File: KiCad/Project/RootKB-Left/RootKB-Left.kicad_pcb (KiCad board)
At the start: 2 copper layers, 137.4 x 107.4 mm, 70 parts, among them J1 OLED-128x32, SW1 Switch, U1 Arduino_Pro_Micro, U2 TRRS

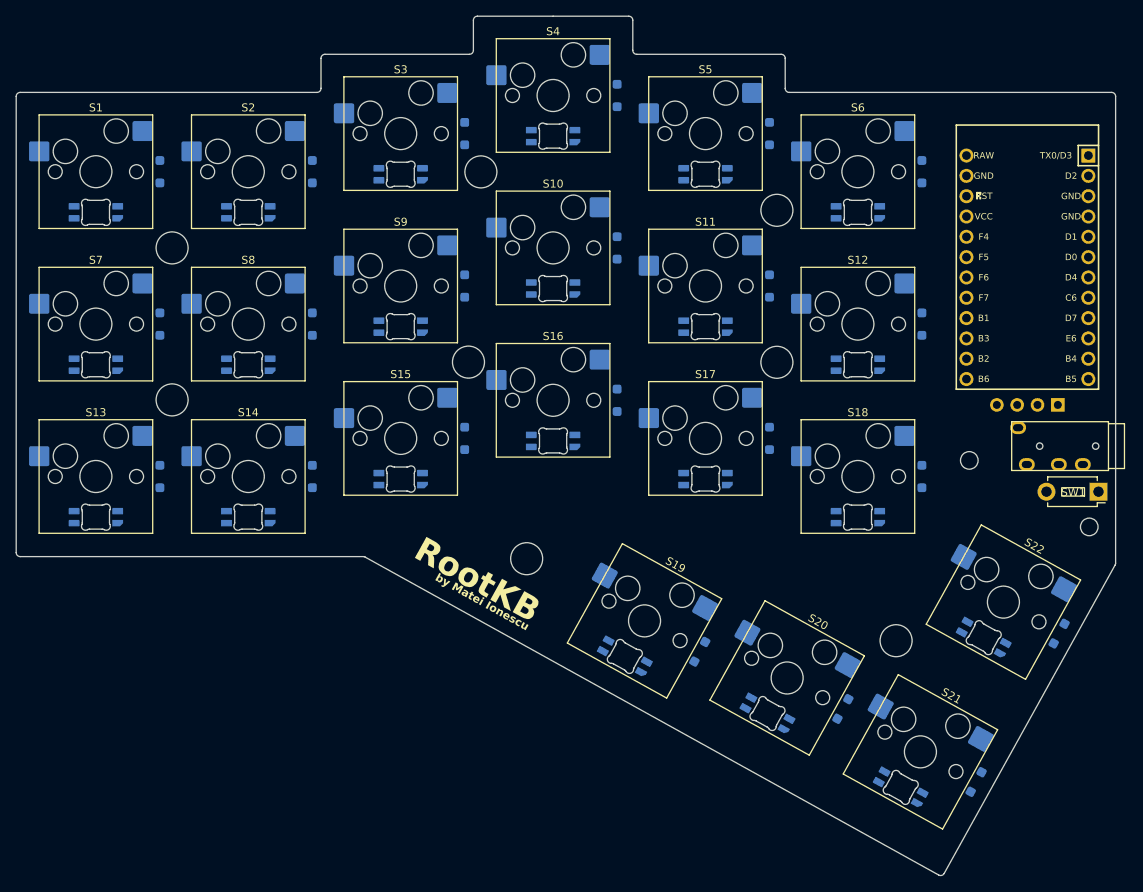
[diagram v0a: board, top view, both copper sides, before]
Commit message: route left
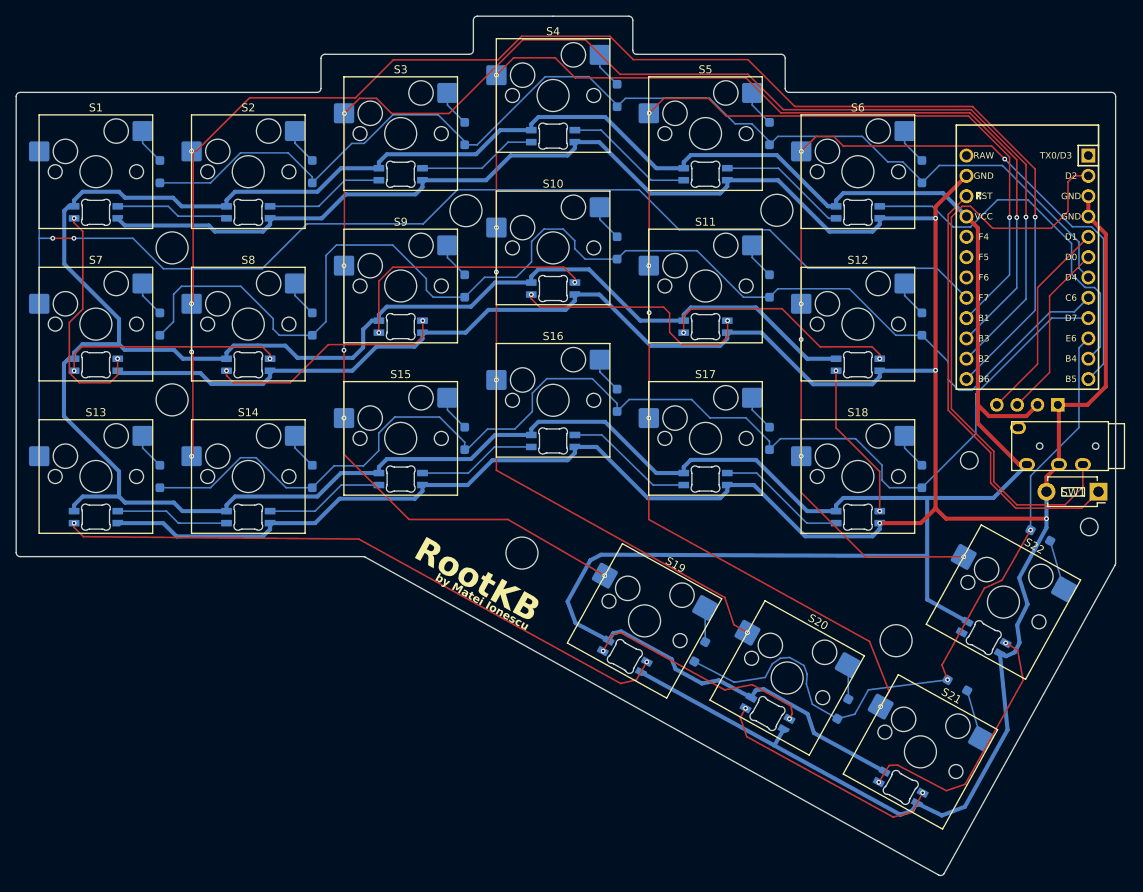
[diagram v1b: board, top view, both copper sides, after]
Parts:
- moved D22 12.5 mm to (203.8, 107.4), turned to -29 degrees
- moved D21 12.3 mm to (193.4, 126.1), turned to -29 degrees
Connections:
- LED1 pad 3: LED -> Net-(LED1-DIN)
- LED11 pad 2: Net-(LED10-DIN) -> Net-(LED11-DOUT)
- LED11 pad 3: Net-(LED11-DIN) -> Net-(LED10-DOUT)
- LED12 pad 2: Net-(LED11-DIN) -> Net-(LED12-DOUT)
- LED12 pad 3: Net-(LED12-DIN) -> Net-(LED11-DOUT)
- LED13 pad 4: unconnected-(LED13-VSS-Pad4) -> GND
- LED14 pad 2: Net-(LED14-DOUT) -> Net-(LED13-DIN)
- LED14 pad 3: Net-(LED13-DOUT) -> Net-(LED14-DIN)
- LED14 pad 4: unconnected-(LED14-VSS-Pad4) -> GND
- LED15 pad 2: Net-(LED15-DOUT) -> Net-(LED14-DIN)
- LED15 pad 3: Net-(LED14-DOUT) -> Net-(LED15-DIN)
- LED16 pad 2: Net-(LED16-DOUT) -> Net-(LED15-DIN)
- LED16 pad 3: Net-(LED15-DOUT) -> Net-(LED16-DIN)
- LED17 pad 2: Net-(LED17-DOUT) -> Net-(LED16-DIN)
- LED17 pad 3: Net-(LED16-DOUT) -> Net-(LED17-DIN)
- LED18 pad 2: Net-(LED18-DOUT) -> Net-(LED17-DIN)
- LED18 pad 3: Net-(LED17-DOUT) -> Net-(LED12-DOUT)
- LED19 pad 2: unconnected-(LED19-DOUT-Pad2) -> Net-(LED19-DOUT)
- LED19 pad 3: Net-(LED19-DIN) -> Net-(LED13-DOUT)
- LED2 pad 2: Net-(LED2-DOUT) -> Net-(LED1-DIN)
- LED2 pad 3: Net-(LED1-DOUT) -> Net-(LED2-DIN)
- LED20 pad 2: Net-(LED19-DIN) -> Net-(LED20-DOUT)
- LED20 pad 3: Net-(LED20-DIN) -> Net-(LED19-DOUT)
- LED21 pad 2: Net-(LED20-DIN) -> Net-(LED21-DOUT)
- LED21 pad 3: Net-(LED21-DIN) -> Net-(LED20-DOUT)
- LED22 pad 2: Net-(LED21-DIN) -> unconnected-(LED22-DOUT-Pad2)
- LED22 pad 3: Net-(LED18-DOUT) -> Net-(LED21-DOUT)
- LED3 pad 2: Net-(LED3-DOUT) -> Net-(LED2-DIN)
- LED3 pad 3: Net-(LED2-DOUT) -> Net-(LED3-DIN)
- LED4 pad 2: Net-(LED4-DOUT) -> Net-(LED3-DIN)
- LED4 pad 3: Net-(LED3-DOUT) -> Net-(LED4-DIN)
- LED5 pad 2: Net-(LED5-DOUT) -> Net-(LED4-DIN)
- LED5 pad 3: Net-(LED4-DOUT) -> Net-(LED5-DIN)
- LED6 pad 2: Net-(LED12-DIN) -> Net-(LED5-DIN)
- LED6 pad 3: Net-(LED5-DOUT) -> LED
- LED7 pad 2: Net-(LED13-DIN) -> Net-(LED7-DOUT)
- LED7 pad 3: Net-(LED7-DIN) -> Net-(LED1-DOUT)
- LED8 pad 2: Net-(LED7-DIN) -> Net-(LED8-DOUT)
- LED8 pad 3: Net-(LED8-DIN) -> Net-(LED7-DOUT)
- LED9 pad 2: Net-(LED8-DIN) -> Net-(LED10-DIN)
- LED9 pad 3: Net-(LED10-DOUT) -> Net-(LED8-DOUT)
- U1 pad 13: Column 4 -> Column 1
- U1 pad 14: Column 3 -> Column 2
- U1 pad 15: Column 2 -> Column 3
- U1 pad 16: Column 1 -> Column 4
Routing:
- net VCC: track 0.00 -> 579.8 mm
- net GND: track 0.00 -> 544.0 mm, vias 0 -> 4
- net Column 2: track 0.00 -> 205.0 mm, vias 0 -> 6
- net Column 1: track 0.00 -> 186.6 mm, vias 0 -> 5
- net Column 3: track 0.00 -> 184.2 mm, vias 0 -> 6
- net Column 0: track 0.00 -> 165.3 mm, vias 0 -> 2
- net Column 4: track 0.00 -> 162.5 mm, vias 0 -> 6
- net Row 1: track 0.00 -> 158.8 mm
- net Row 2: track 0.00 -> 153.4 mm
- net Row 0: track 0.00 -> 144.8 mm
- net Column 5: track 0.00 -> 128.5 mm, vias 0 -> 6
- net Row 3: track 0.00 -> 89.8 mm, vias 0 -> 2
- net Net-(LED13-DOUT): track 0.00 -> 78.6 mm, vias 0 -> 2
- net TRRS_SERIAL: track 0.00 -> 75.0 mm
- net RST: track 0.00 -> 54.9 mm
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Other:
- outline, holes or cut-outs redrawn

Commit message: routing left
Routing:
- net Column 2: track 205.0 -> 203.4 mm

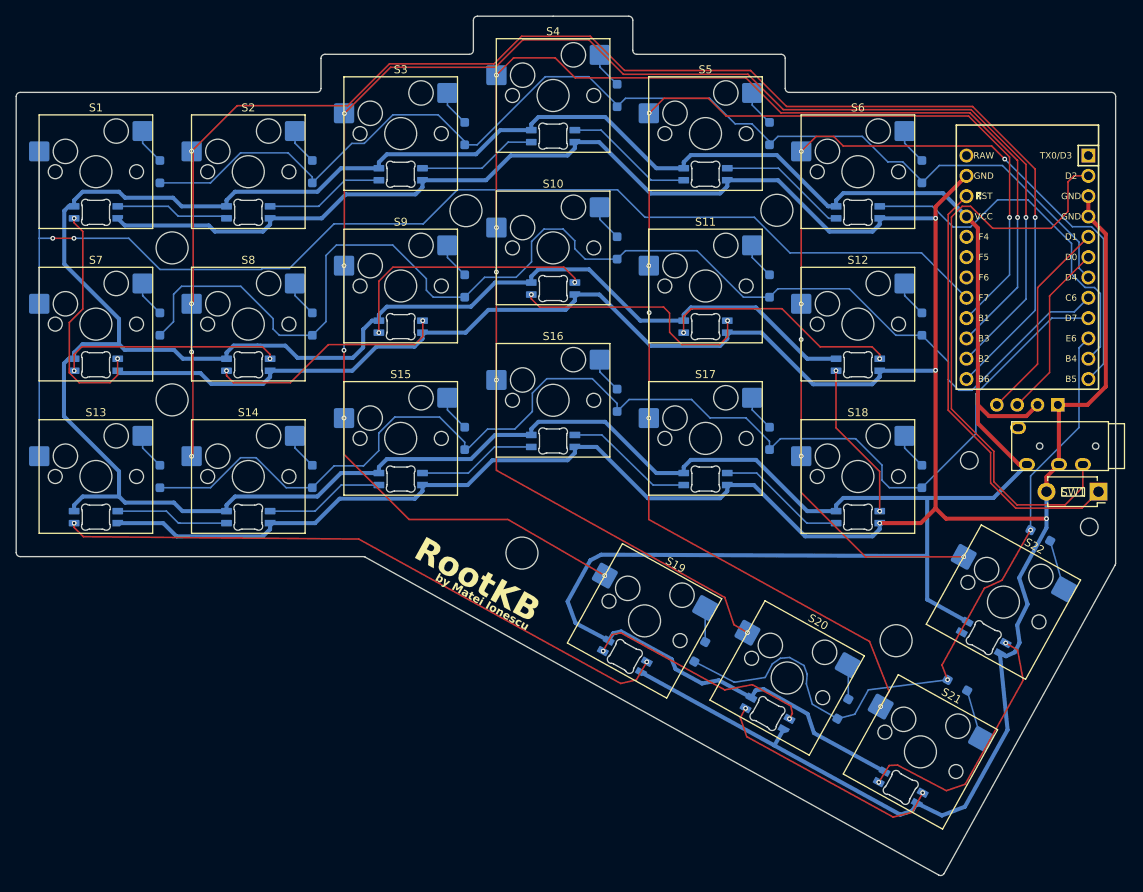
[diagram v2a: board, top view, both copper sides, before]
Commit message: remove reset button
also use real Arduino ProMicro dimensions
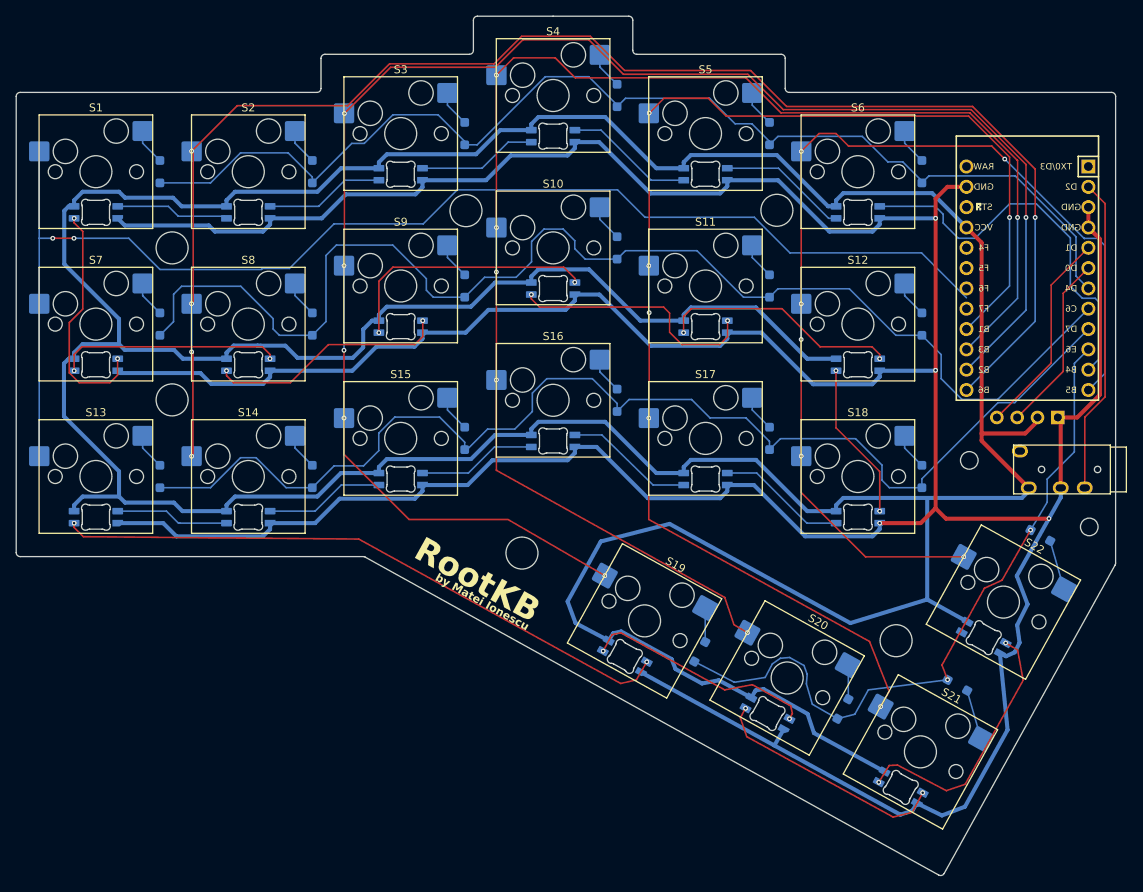
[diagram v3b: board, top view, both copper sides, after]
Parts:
- removed SW1: Switch, ScottoKeebs_Components:Button_MJTP1250
- moved U2 2.93 mm to (212.5, 99.1)
- moved J1 1.57 mm to (196.2, 94.2)
- moved U1 1.37 mm to (202.2, 75.2)
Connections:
- U1 pad 22: RST -> unconnected-(U1-RST-Pad22)
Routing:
- net RST: track 54.9 -> 0.00 mm
- net TRRS_SERIAL: track 75.0 -> 39.5 mm
- net VCC: track 579.8 -> 583.8 mm
- net LED: track 45.9 -> 49.2 mm
- net Row 2: track 153.4 -> 150.6 mm
- net GND: track 544.0 -> 541.6 mm
- net Row 3: track 89.8 -> 88.1 mm
- net Column 2: track 203.4 -> 204.8 mm
- net Column 1: track 186.6 -> 188.0 mm
- net Column 5: track 128.5 -> 129.9 mm
- net Column 4: track 162.5 -> 163.9 mm
- net Column 3: track 184.2 -> 185.6 mm
- net Row 1: track 158.8 -> 159.6 mm

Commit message: fix track
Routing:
- net Column 0: track 165.3 -> 165.9 mm
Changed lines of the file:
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@@
 	)
 	(segment
-		(start 106.53835 74.0075)
-		(end 109.911337 74.0075)
+		(start 89.834292 70.234545)
+		(end 93.734292 74.134545)
+		(width 0.2)
+		(layer "B.Cu")
+		(net 47)
+	)
+	(segment
+		(start 187.834292 72.334545)
+		(end 187.8345 72.334545)
 		(width 0.2)
 		(layer "B.Cu")
@@
 	)
 	(segment
-		(start 82.984292 70.234545)
-		(end 89.834292 70.234545)
+		(start 150.934292 64.184545)
+		(end 154.359292 67.609545)
 		(width 0.2)
 		(layer "B.Cu")
@@
 	(segment
 		(start 172.482221 72.059545)
-		(end 188.93052 72.059545)
+		(end 187.559292 72.059545)
+		(width 0.2)
+		(layer "B.Cu")
+		(net 47)
+	)
+	(segment
+		(start 78.64 70.234545)
+		(end 78.64 78.4225)
+		(width 0.2)
+		(layer "B.Cu")
+		(net 47)
+	)
+	(segment
+		(start 115.484292 68.434545)
+		(end 126.644468 68.434545)
+		(width 0.2)
+		(layer "B.Cu")
+		(net 47)
+	)
+	(segment
+		(start 168.032221 67.609545)
+		(end 172.482221 72.059545)
+		(width 0.2)
+		(layer "B.Cu")
+		(net 47)
+	)
+	(segment
+		(start 130.894468 64.184545)
+		(end 150.934292 64.184545)
+		(width 0.2)
+		(layer "B.Cu")
+		(net 47)
+	)
+	(segment
+		(start 106.411305 74.134545)
+		(end 106.53835 74.0075)
+		(width 0.2)
+		(layer "B.Cu")
+		(net 47)
+	)
+	(segment
+		(start 82.984292 70.234545)
+		(end 89.834292 70.234545)
 		(width 0.2)
 		(layer "B.Cu")
@@
 	)
 	(segment
-		(start 109.911337 74.0075)
-		(end 115.484292 68.434545)
+		(start 187.8345 72.334545)
+		(end 194.5445 79.044545)
 		(width 0.2)
 		(layer "B.Cu")
@@
 	)
 	(segment
-		(start 78.64 70.234545)
-		(end 78.64 78.4225)
+		(start 109.911337 74.0075)
+		(end 115.484292 68.434545)
 		(width 0.2)
 		(layer "B.Cu")
@@
 	)
 	(segment
-		(start 130.894468 64.184545)
-		(end 150.934292 64.184545)
-		(width 0.2)
-		(layer "B.Cu")
-		(net 47)
-	)
-	(segment
-		(start 168.032221 67.609545)
-		(end 172.482221 72.059545)
-		(width 0.2)
-		(layer "B.Cu")
-		(net 47)
-	)
-	(segment
-		(start 188.93052 72.059545)
-		(end 194.5445 77.673525)
-		(width 0.2)
-		(layer "B.Cu")
-		(net 47)
-	)
-	(segment
 		(start 78.64 78.4225)
 		(end 78.64 97.4725)
@@
 	)
 	(segment
-		(start 89.834292 70.234545)
-		(end 93.734292 74.134545)
+		(start 106.53835 74.0075)
+		(end 109.911337 74.0075)
 		(width 0.2)
 		(layer "B.Cu")
@@
 	)
 	(segment
-		(start 115.484292 68.434545)
-		(end 126.644468 68.434545)
-		(width 0.2)
-		(layer "B.Cu")
-		(net 47)
-	)
-	(segment
-		(start 106.411305 74.134545)
-		(end 106.53835 74.0075)
+		(start 126.644468 68.434545)
+		(end 130.894468 64.184545)
 		(width 0.2)
 		(layer "B.Cu")
@@
 	)
 	(segment
-		(start 150.934292 64.184545)
-		(end 154.359292 67.609545)
+		(start 187.559292 72.059545)
+		(end 187.834292 72.334545)
 		(width 0.2)
 		(layer "B.Cu")
-		(net 47)
-	)
-	(segment
-		(start 126.644468 68.434545)
-		(end 130.894468 64.184545)
-		(width 0.2)
-		(layer "B.Cu")

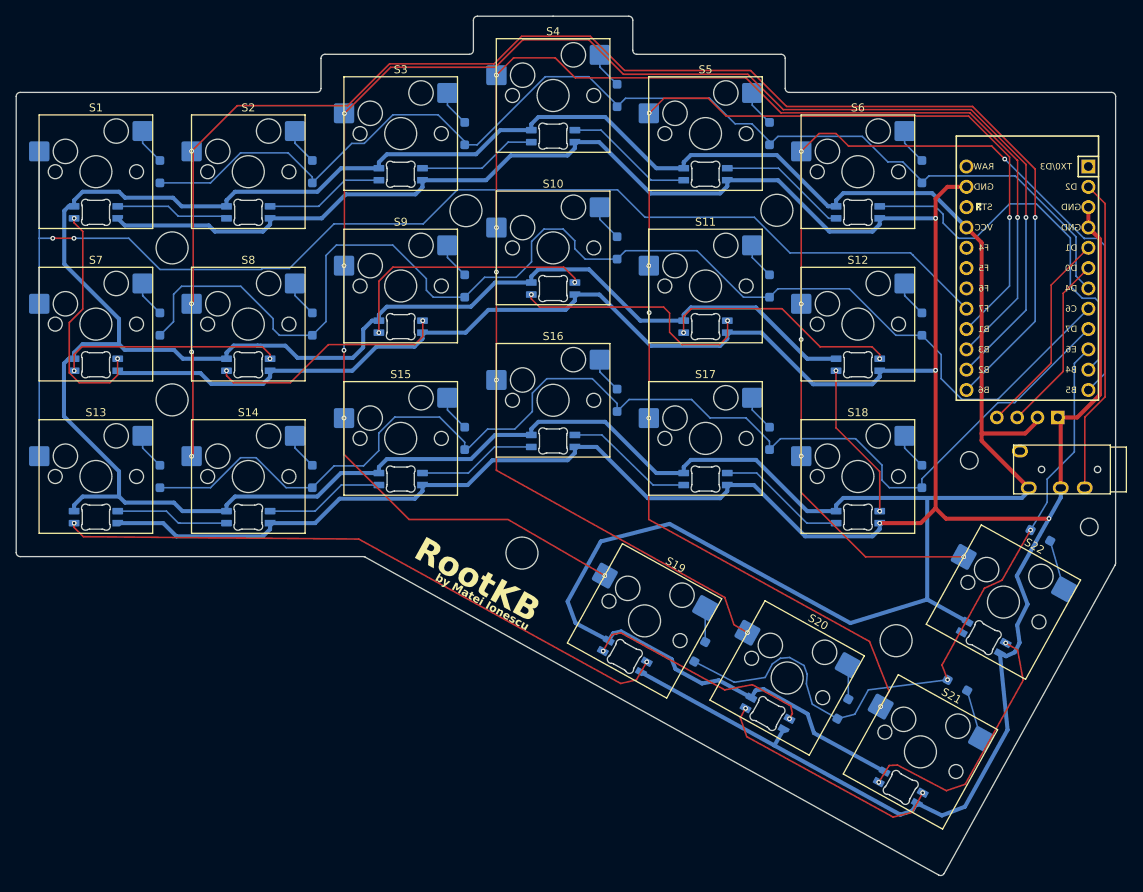
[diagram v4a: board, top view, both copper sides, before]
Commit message: move vias away from pads
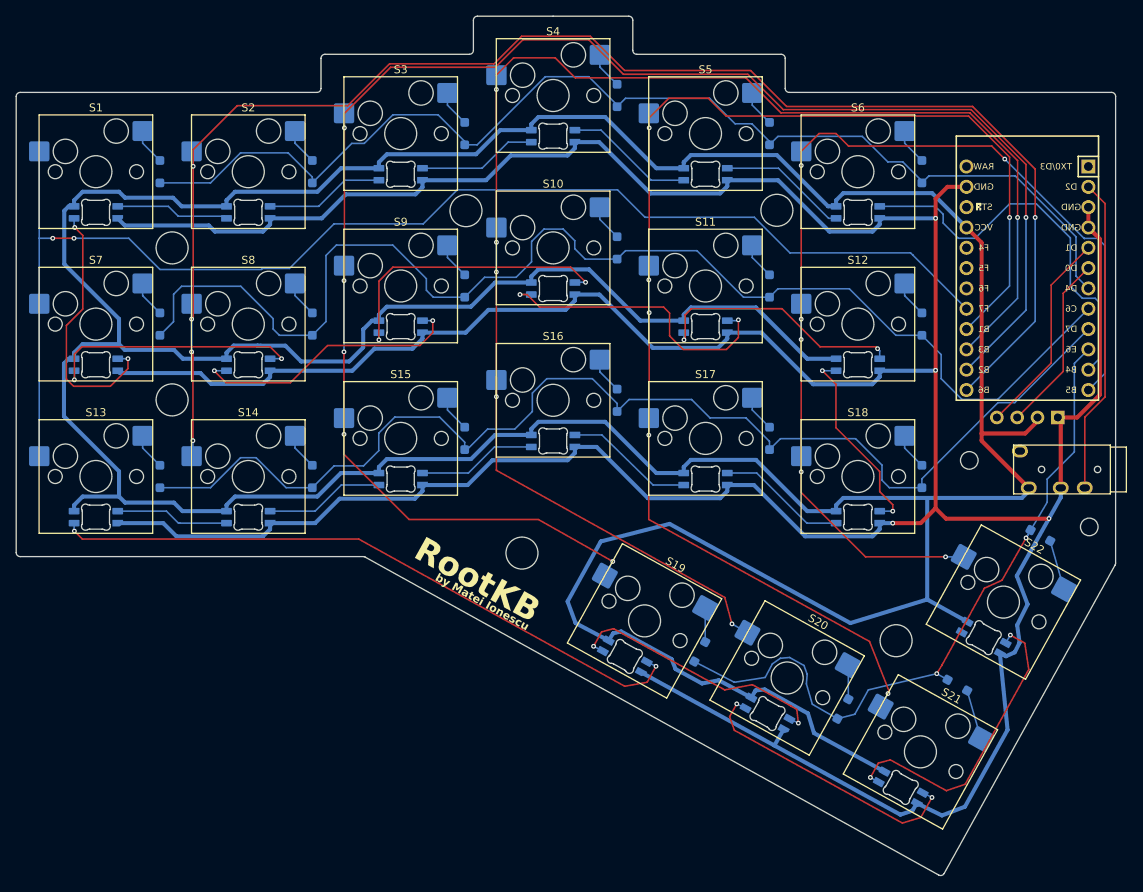
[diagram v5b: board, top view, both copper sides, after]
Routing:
- net Column 2: track 204.8 -> 213.0 mm
- net Column 3: track 185.6 -> 193.5 mm
- net Net-(LED10-DOUT): track 31.3 -> 37.5 mm
- net Column 5: track 129.9 -> 135.5 mm
- net Net-(LED20-DOUT): track 30.0 -> 35.4 mm
- net Column 4: track 163.9 -> 169.3 mm
- net Net-(LED8-DOUT): track 29.9 -> 34.8 mm
- net Net-(LED21-DOUT): track 33.4 -> 38.3 mm
- net Net-(LED7-DOUT): track 27.9 -> 32.7 mm
- net Net-(LED12-DOUT): track 19.8 -> 24.6 mm
- net Net-(LED19-DOUT): track 29.1 -> 33.7 mm
- net Net-(LED10-DIN): track 32.8 -> 36.9 mm
- net Column 1: track 188.0 -> 191.6 mm
- net Net-(LED1-DOUT): track 29.5 -> 32.9 mm
- net Net-(LED13-DOUT): track 78.6 -> 81.4 mm
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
